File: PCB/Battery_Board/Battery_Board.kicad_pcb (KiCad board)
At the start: 2 copper layers, 90 x 83 mm, 3 parts

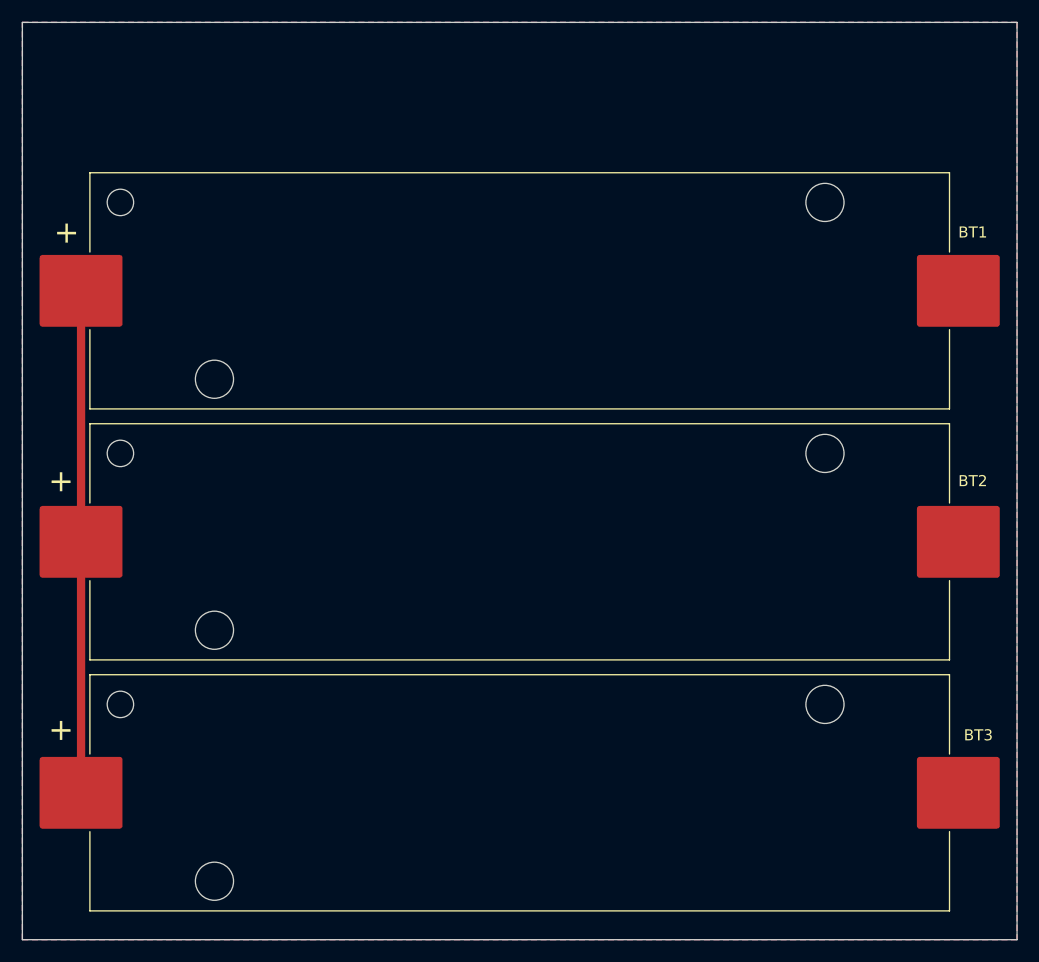
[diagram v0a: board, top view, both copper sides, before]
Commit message: changed battery config to series, added graphic
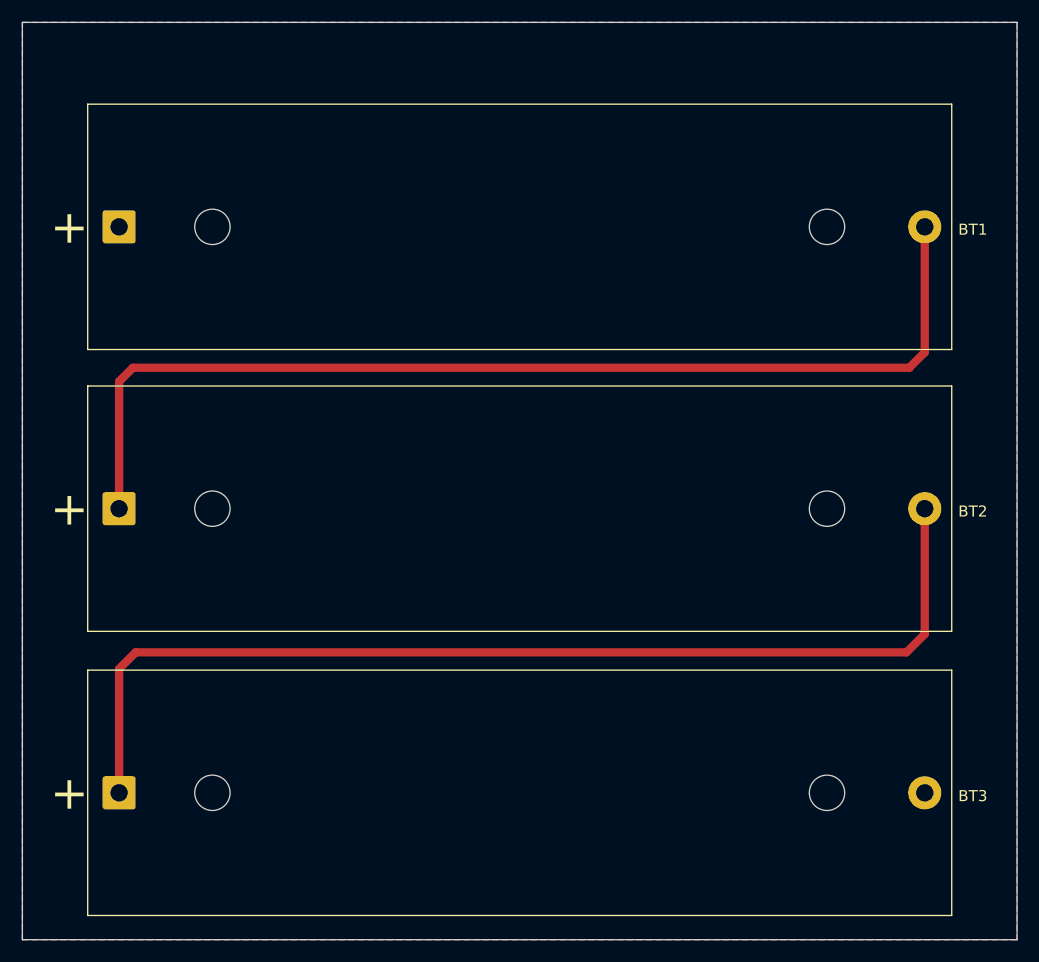
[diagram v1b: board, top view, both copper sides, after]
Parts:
- added G***: LOGO, LOGO, B.Cu at (117.0, 83.0)
- BT1, BT2, BT3: footprint Battery:BatteryHolder_Keystone_1042_1x18650 -> Battery:BatteryHolder_MPD_BK-18650-PC2
- moved BT1 36.7 mm to (80.8, 60.0)
- moved BT2 36.4 mm to (80.8, 85.5)
- moved BT3 36.2 mm to (80.8, 111.2)
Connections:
- BT1 pad 2: GND -> Net-(BT1--)
- BT2 pad 1: VBUS -> Net-(BT1--)
- BT2 pad 2: GND -> Net-(BT2--)
- BT3 pad 1: VBUS -> Net-(BT2--)
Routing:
- net Net-(BT1--): track 0.00 -> 96.8 mm
- net Net-(BT2--): track 0.00 -> 96.8 mm
- net VBUS: track 45.4 -> 0.00 mm

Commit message: Added Connector
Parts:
- added J1: SE2-30, SE2-30:SE2-30, F.Cu at (217.5, 46.0)
- moved G*** 101.2 mm to (218.0, 90.0)
- moved BT1 101.2 mm to (181.8, 67.0)
- moved BT2 101.2 mm to (181.8, 92.5)
- moved BT3 101.2 mm to (181.8, 118.2)
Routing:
- net VBUS: track 0.00 -> 94.0 mm, vias 0 -> 1
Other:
- board size 90 x 83 mm -> 90 x 90 mm

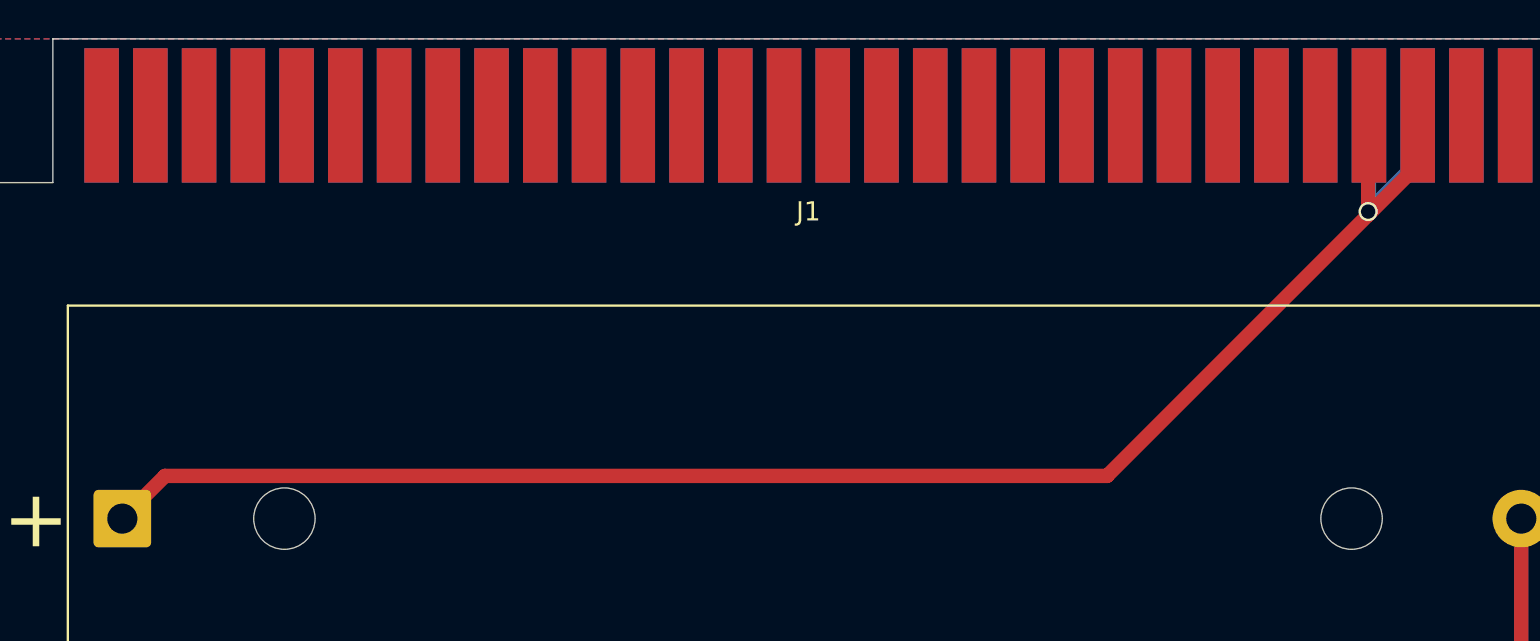
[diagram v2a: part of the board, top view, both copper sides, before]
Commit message: added design rules
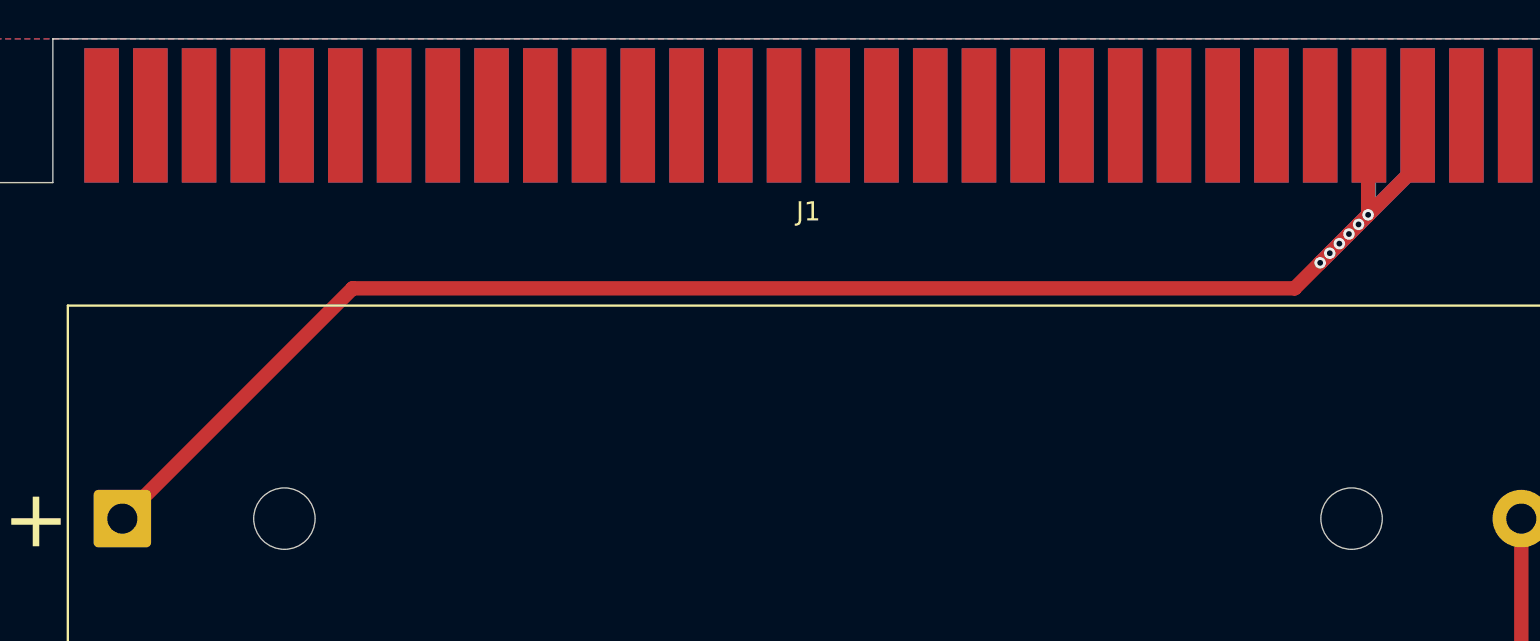
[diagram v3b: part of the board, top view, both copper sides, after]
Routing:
- net VBUS: track 94.0 -> 97.8 mm, vias 1 -> 6
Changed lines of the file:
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@@
+	)
+	(segment
+		(start 246.17 51.67)
+		(end 246.67 51.17)
+		(width 0.75)
+		(layer "F.Cu")
+		(net 1)
 	)
 	(segment
@@
 	)
 	(segment
-		(start 233.066 64.774)
-		(end 246.67 51.17)
-		(width 0.75)
-		(layer "F.Cu")
-		(net 1)
-	)
-	(segment
-		(start 183.977029 64.774)
-		(end 233.066 64.774)
-		(width 0.75)
-		(layer "F.Cu")
-		(net 1)
-	)
-	(segment
-		(start 181.751029 67)
-		(end 183.977029 64.774)
+		(start 193.751029 55)
+		(end 242.84 55)
+		(width 0.75)
+		(layer "F.Cu")
+		(net 1)
+	)
+	(segment
+		(start 245.17 52.67)
+		(end 245.67 52.17)
+		(width 0.75)
+		(layer "F.Cu")
+		(net 1)
+	)
+	(segment
+		(start 242.84 55)
+		(end 244.17 53.67)
+		(width 0.75)
+		(layer "F.Cu")
+		(net 1)
+	)
+	(segment
+		(start 244.17 53.67)
+		(end 244.67 53.17)
+		(width 0.75)
+		(layer "F.Cu")
+		(net 1)
+	)
+	(segment
+		(start 245.67 52.17)
+		(end 246.17 51.67)
 		(width 0.75)
 		(layer "F.Cu")
@@
 		(net 1)
 	)
-	(via blind
-		(at 246.67 51)
-		(size 1)
-		(drill 0.75)
-		(layers "F.Cu" "B.Cu")
+	(segment
+		(start 181.751029 67)
+		(end 193.751029 55)
+		(width 0.75)
+		(layer "F.Cu")
+		(net 1)
+	)
+	(segment
+		(start 244.67 53.17)
+		(end 245.17 52.67)
+		(width 0.75)
+		(layer "F.Cu")
+		(net 1)
+	)
+	(via
+		(at 246.17 51.67)
+		(size 0.6)
+		(drill 0.3)
+		(layers "F.Cu" "B.Cu")
+		(net 1)
+	)
+	(via
+		(at 246.67 51.17)
+		(size 0.6)
+		(drill 0.3)
+		(layers "F.Cu" "B.Cu")
+		(net 1)
+	)
+	(via
+		(at 245.17 52.67)
+		(size 0.6)
+		(drill 0.3)
+		(layers "F.Cu" "B.Cu")
+		(net 1)
+	)
+	(via
+		(at 245.67 52.17)
+		(size 0.6)
+		(drill 0.3)
+		(layers "F.Cu" "B.Cu")
+		(net 1)
+	)
+	(via
+		(at 244.17 53.67)
+		(size 0.6)
+		(drill 0.3)
+		(layers "F.Cu" "B.Cu")
+		(net 1)
+	)
+	(via
+		(at 244.67 53.17)
+		(size 0.6)
+		(drill 0.3)
+		(layers "F.Cu" "B.Cu")
+		(net 1)
+	)
+	(segment
+		(start 246.71 45.99)
+		(end 246.71 51.13)
+		(width 0.75)
+		(layer "B.Cu")
+		(net 1)
+	)
+	(segment
+		(start 249.25 48.59)
+		(end 246.71 51.13)
+		(width 0.75)
+		(layer "B.Cu")
+		(net 1)
+	)
+	(segment
+		(start 246.71 51.13)
+		(end 244.17 53.67)
+		(width 0.75)
+		(layer "B.Cu")
 		(net 1)
 	)
 	(segment
 		(start 249.25 45.99)
-		(end 249.25 48.42)
-		(width 0.75)
-		(layer "B.Cu")
-		(net 1)
-	)
-	(segment
-		(start 246.71 50.96)
-		(end 246.67 51)
-		(width 0.75)
-		(layer "B.Cu")
-		(net 1)
-	)
-	(segment
-		(start 249.25 48.42)
-		(end 246.67 51)
-		(width 0.75)
-		(layer "B.Cu")
-		(net 1)
-	)
-	(segment
-		(start 246.71 45.99)
-		(end 246.71 50.96)
+		(end 249.25 48.59)
 		(width 0.75)
 		(layer "B.Cu")
@@
 	)
 	(zone
+		(net 4)
+		(net_name "Net-(BT2--)")
+		(layer "F.Cu")
+		(name "$teardrop_padvia$")
+		(hatch none 0.1)
+		(priority 30004)
+		(attr
+			(teardrop
+				(type padvia)
+			)
+		)
+		(connect_pads yes
+			(clearance 0)
+		)
+		(min_thickness 0.0254)
+		(filled_areas_thickness no)
+		(fill yes
+			(thermal_gap 0.5)
+			(thermal_bridge_width 0.5)
+			(island_removal_mode 1)
+			(island_area_min 10)
+		)
+		(polygon
+			(pts
+				(xy 182.126029 115.710001) (xy 181.376029 115.710001) (xy 180.751029 116.71) (xy 181.751029 118.211)
+				(xy 182.751029 116.71)
+			)
+		)
+	)
+	(zone
+		(net 1)
+		(net_name "VBUS")
+		(layer "F.Cu")
+		(name "$teardrop_padvia$")
+		(hatch none 0.1)
+		(priority 30000)
+		(attr
+			(teardrop
+				(type padvia)
+			)
+		)
+		(connect_pads yes
+			(clearance 0)
+		)
+		(min_thickness 0.0254)
+		(filled_areas_thickness no)
+		(fill yes
+			(thermal_gap 0.5)
+			(thermal_bridge_width 0.5)
+			(island_removal_mode 1)
+			(island_area_min 10)
+		)
+		(polygon
+			(pts
+				(xy 184.150077 65.131282) (xy 183.619747 64.600952) (xy 181.836814 65.5) (xy 181.750322 67.000707)
+				(xy 183.251028 66.914214)
+			)
+		)
+	)
+	(zone
 		(net 3)
 		(net_name "Net-(BT1--)")
@@
 		(name "$teardrop_padvia$")
 		(hatch none 0.1)
-		(priority 30002)
+		(priority 30001)
 		(attr
 			(teardrop
@@
 	)
 	(zone
+		(net 3)
+		(net_name "Net-(BT1--)")
+		(layer "F.Cu")
+		(name "$teardrop_padvia$")
+		(hatch none 0.1)
+		(priority 30003)
+		(attr
+			(teardrop
+				(type padvia)
+			)
+		)
+		(connect_pads yes
+			(clearance 0)
+		)
+		(min_thickness 0.0254)
+		(filled_areas_thickness no)
+		(fill yes
+			(thermal_gap 0.5)
+			(thermal_bridge_width 0.5)
+			(island_removal_mode 1)
+			(island_area_min 10)
+		)
+		(polygon
+			(pts
+				(xy 182.126029 90.000001) (xy 181.376029 90.000001) (xy 180.751029 91) (xy 181.751029 92.501) (xy 182.751029 91)
+			)
+		)
+	)
+	(zone
 		(net 4)
 		(net_name "Net-(BT2--)")
@@
 		(name "$teardrop_padvia$")
 		(hatch none 0.1)
-		(priority 30001)
+		(priority 30002)
 		(attr
 			(teardrop
@@
 			)
 		)
-	)
-	(zone
-		(net 4)
-		(net_name "Net-(BT2--)")
-		(layer "F.Cu")
-		(name "$teardrop_padvia$")
-		(hatch none 0.1)
-		(priority 30004)
-		(attr
-			(teardrop
-				(type padvia)
-			)
-		)
-		(connect_pads yes
-			(clearance 0)
-		)
-		(min_thickness 0.0254)
-		(filled_areas_thickness no)
-		(fill yes
-			(thermal_gap 0.5)
-			(thermal_bridge_width 0.5)
-			(island_removal_mode 1)
-			(island_area_min 10)
-		)
-		(polygon
-			(pts
-				(xy 182.126029 115.710001) (xy 181.376029 115.710001) (xy 180.751029 116.71) (xy 181.751029 118.211)
-				(xy 182.751029 116.71)
-			)
-		)
-	)
-	(zone
-		(net 1)
-		(net_name "VBUS")
-		(layer "F.Cu")
-		(name "$teardrop_padvia$")
-		(hatch none 0.1)
-		(priority 30000)
-		(attr
-			(teardrop
-				(type padvia)
-			)
-		)
-		(connect_pads yes
-			(clearance 0)
-		)
-		(min_thickness 0.0254)
-		(filled_areas_thickness no)
-		(fill yes
-			(thermal_gap 0.5)
-			(thermal_bridge_width 0.5)
-			(island_removal_mode 1)
-			(island_area_min 10)
-		)
-		(polygon
-			(pts
-				(xy 184.150077 65.131282) (xy 183.619747 64.600952) (xy 181.836814 65.5) (xy 181.750322 67.000707)
-				(xy 183.251028 66.914214)
-			)
-		)
-	)
-	(zone
-		(net 3)
-		(net_name "Net-(BT1--)")
-		(layer "F.Cu")
-		(name "$teardrop_padvia$")
-		(hatch none 0.1)
-		(priority 30003)
-		(attr
-			(teardrop
-				(type padvia)
-			)
-		)
-		(connect_pads yes
-			(clearance 0)
-		)
-		(min_thickness 0.0254)
-		(filled_areas_thickness no)
-		(fill yes
-			(thermal_gap 0.5)
-			(thermal_bridge_width 0.5)
-			(island_removal_mode 1)
-			(island_area_min 10)
-		)
-		(polygon
-			(pts
-				(xy 182.126029 90.000001) (xy 181.376029 90.000001) (xy 180.751029 91) (xy 181.751029 92.501) (xy 182.751029 91)
-			)
-		)

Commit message: update schematics
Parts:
- removed G***: LOGO, LOGO
